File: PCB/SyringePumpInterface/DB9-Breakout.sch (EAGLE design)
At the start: 3 parts, among them J2 AUDIO_JACK_3.5MM_PTH

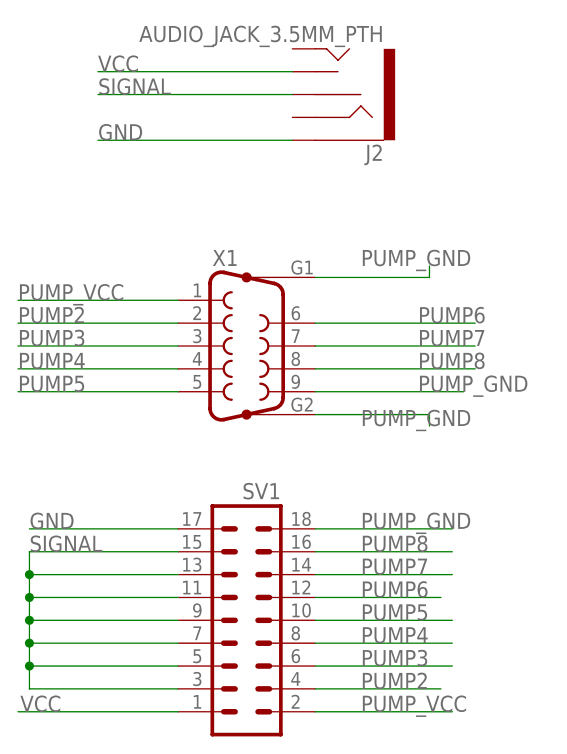
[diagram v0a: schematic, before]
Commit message: New mouse-scale nose poke foodwell designs added. Also a flexible PCB beam break pcb. Also updated DB9 breakout for the syringe pump that has a jumper to choose the pulse pin.
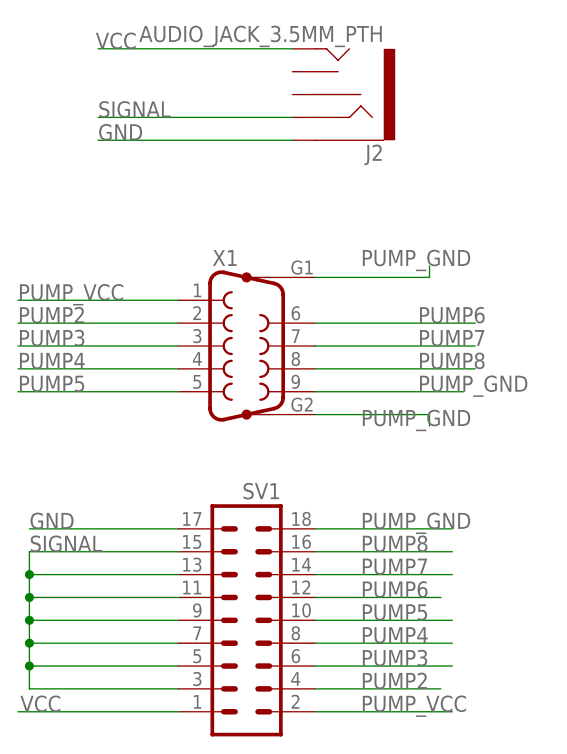
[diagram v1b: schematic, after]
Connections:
- net SIGNAL: now also J2.RING; no longer J2.RSH
- net VCC: now also J2.TIP; no longer J2.TSH
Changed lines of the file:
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@@
 <?xml version="1.0" encoding="utf-8"?>
 <!DOCTYPE eagle SYSTEM "eagle.dtd">
-<eagle version="9.4.2">
+<eagle version="9.5.2">
 <drawing>
 <settings>
@@
 <layer number="255" name="routoute" color="7" fill="1" visible="yes" active="yes"/>
 </layers>
-<schematic xreflabel="%N (%S.%C%R)" xrefpart="/%S.%C%R">
+<schematic xreflabel="%F%N/%S.%C%R" xrefpart="/%S.%C%R">
 <attributes>
 </attributes>
@@
 </segment>
 <segment>
-<pinref part="J2" gate="G$1" pin="RSH"/>
-<wire x1="33.02" y1="74.93" x2="11.43" y2="74.93" width="0.1524" layer="91"/>
-<label x="11.43" y="74.93" size="1.778" layer="95"/>
+<pinref part="J2" gate="G$1" pin="RING"/>
+<wire x1="33.02" y1="72.39" x2="11.43" y2="72.39" width="0.1524" layer="91"/>
+<label x="11.43" y="72.39" size="1.778" layer="95"/>
 </segment>
 </net>
 <net name="VCC" class="0">
-<segment>
-<pinref part="J2" gate="G$1" pin="TSH"/>
-<wire x1="33.02" y1="77.47" x2="11.43" y2="77.47" width="0.1524" layer="91"/>
-<label x="11.43" y="77.47" size="1.778" layer="95"/>
-</segment>
 <segment>
 <pinref part="SV1" gate="G$1" pin="1"/>
@@
 <label x="2.794" y="6.35" size="1.778" layer="95"/>
 </segment>
-</net>
+<segment>
+<pinref part="J2" gate="G$1" pin="TIP"/>
+<wire x1="33.02" y1="80.01" x2="11.43" y2="80.01" width="0.1524" layer="91"/>
+<label x="11.176" y="80.01" size="1.778" layer="95"/>
+</segment>
+</net>
